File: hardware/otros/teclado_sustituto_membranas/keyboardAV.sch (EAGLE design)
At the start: 98 parts, among them IC1 74HC32, IC2 74LS244DW

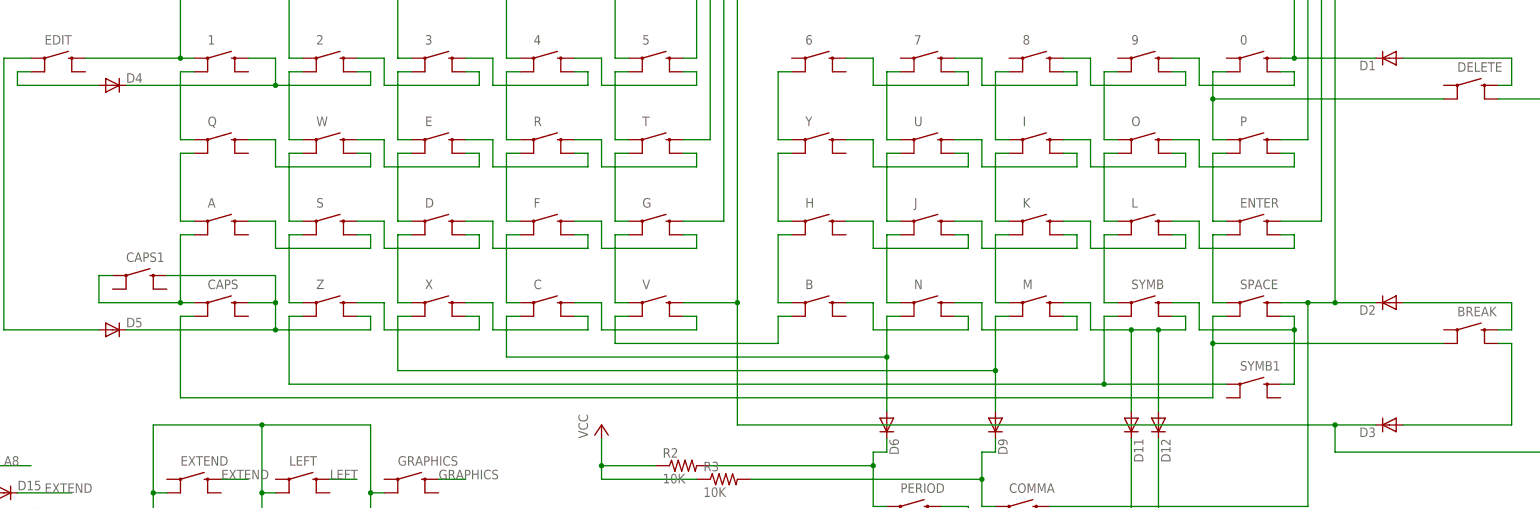
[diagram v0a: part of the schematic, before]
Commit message: 
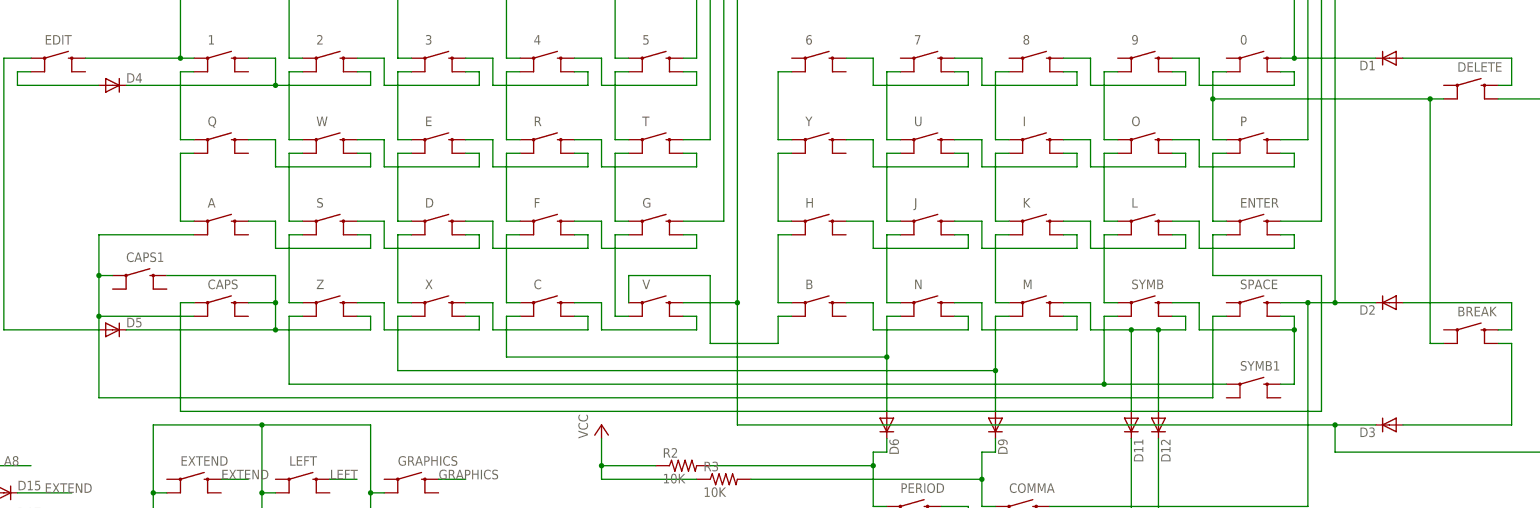
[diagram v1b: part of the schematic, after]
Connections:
- removed net N$52: ENTER.3, SPACE.1
- removed net N$8: A.3, CAPS.1, CAPS1.1
- new net N$91: A.3, CAPS.3, CAPS1.1, SPACE.3
- net N$19: now also V.1; no longer V.3
- net N$28: now also V.3; no longer V.1
- net N$54: now also BREAK.3
- net N$9: now also CAPS.1, ENTER.3; no longer BREAK.3, CAPS.3, SPACE.3

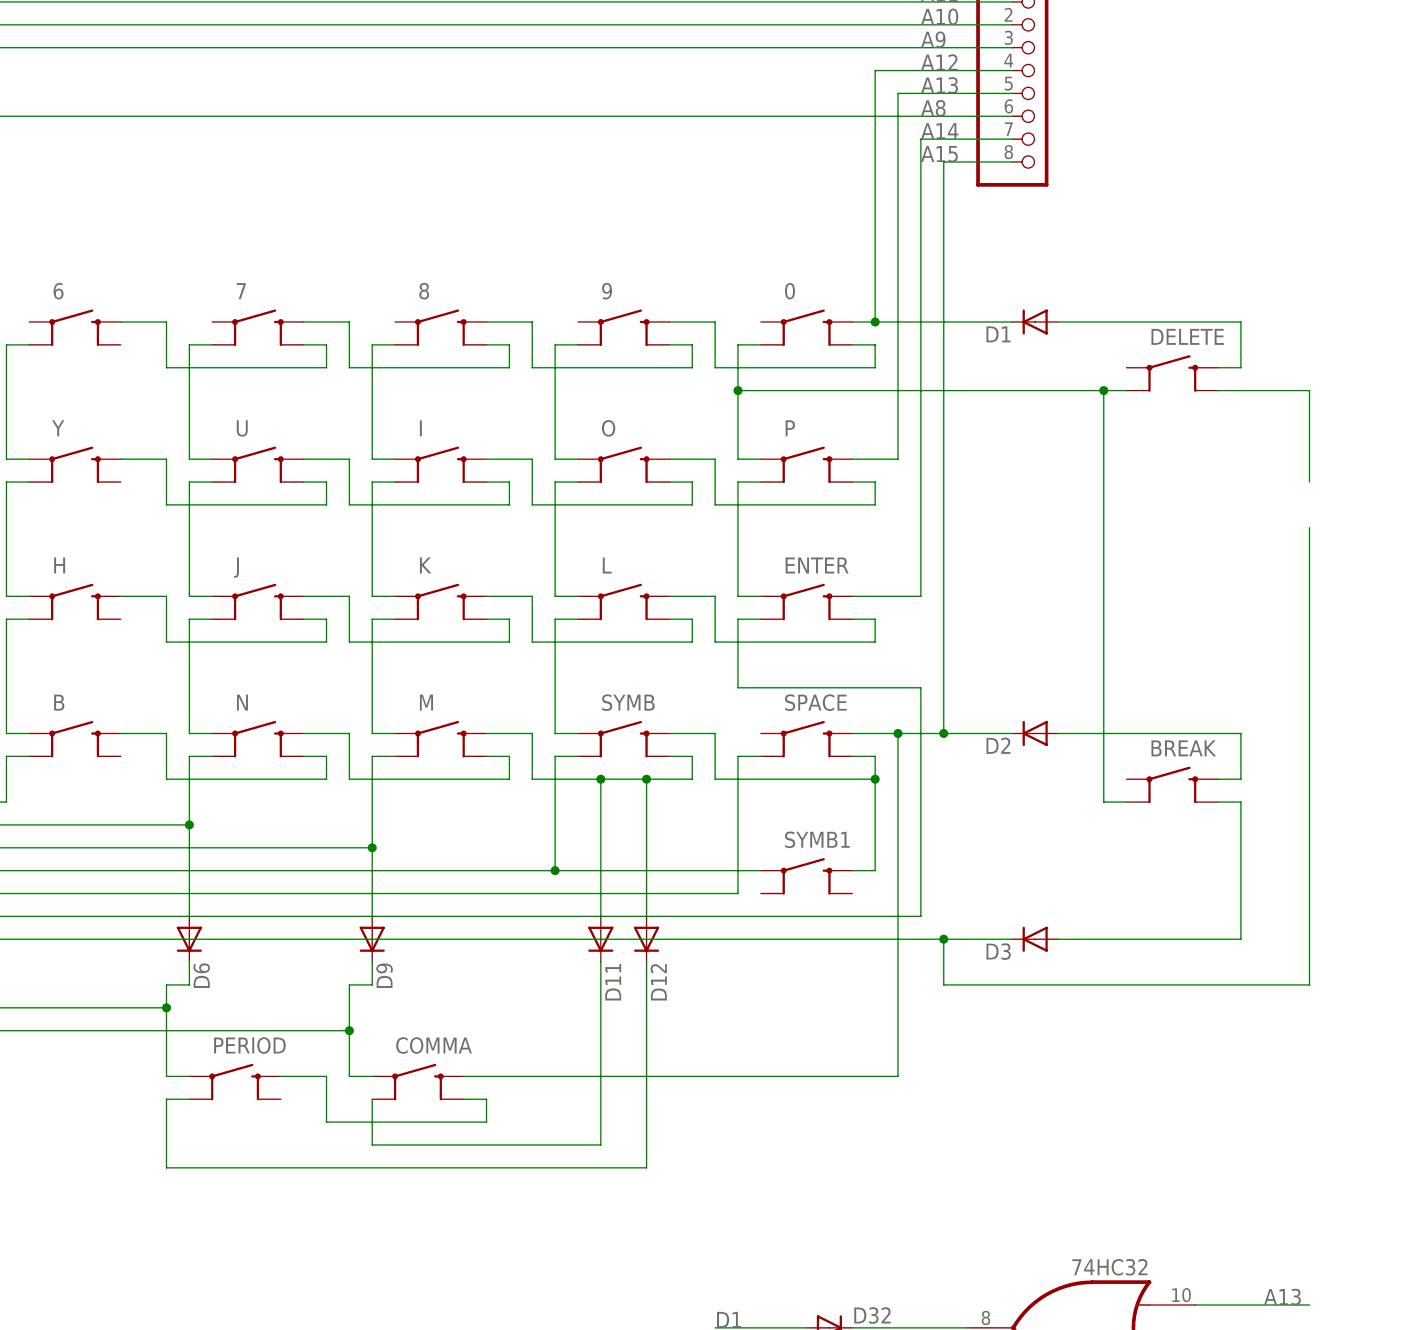
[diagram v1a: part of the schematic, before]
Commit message: 
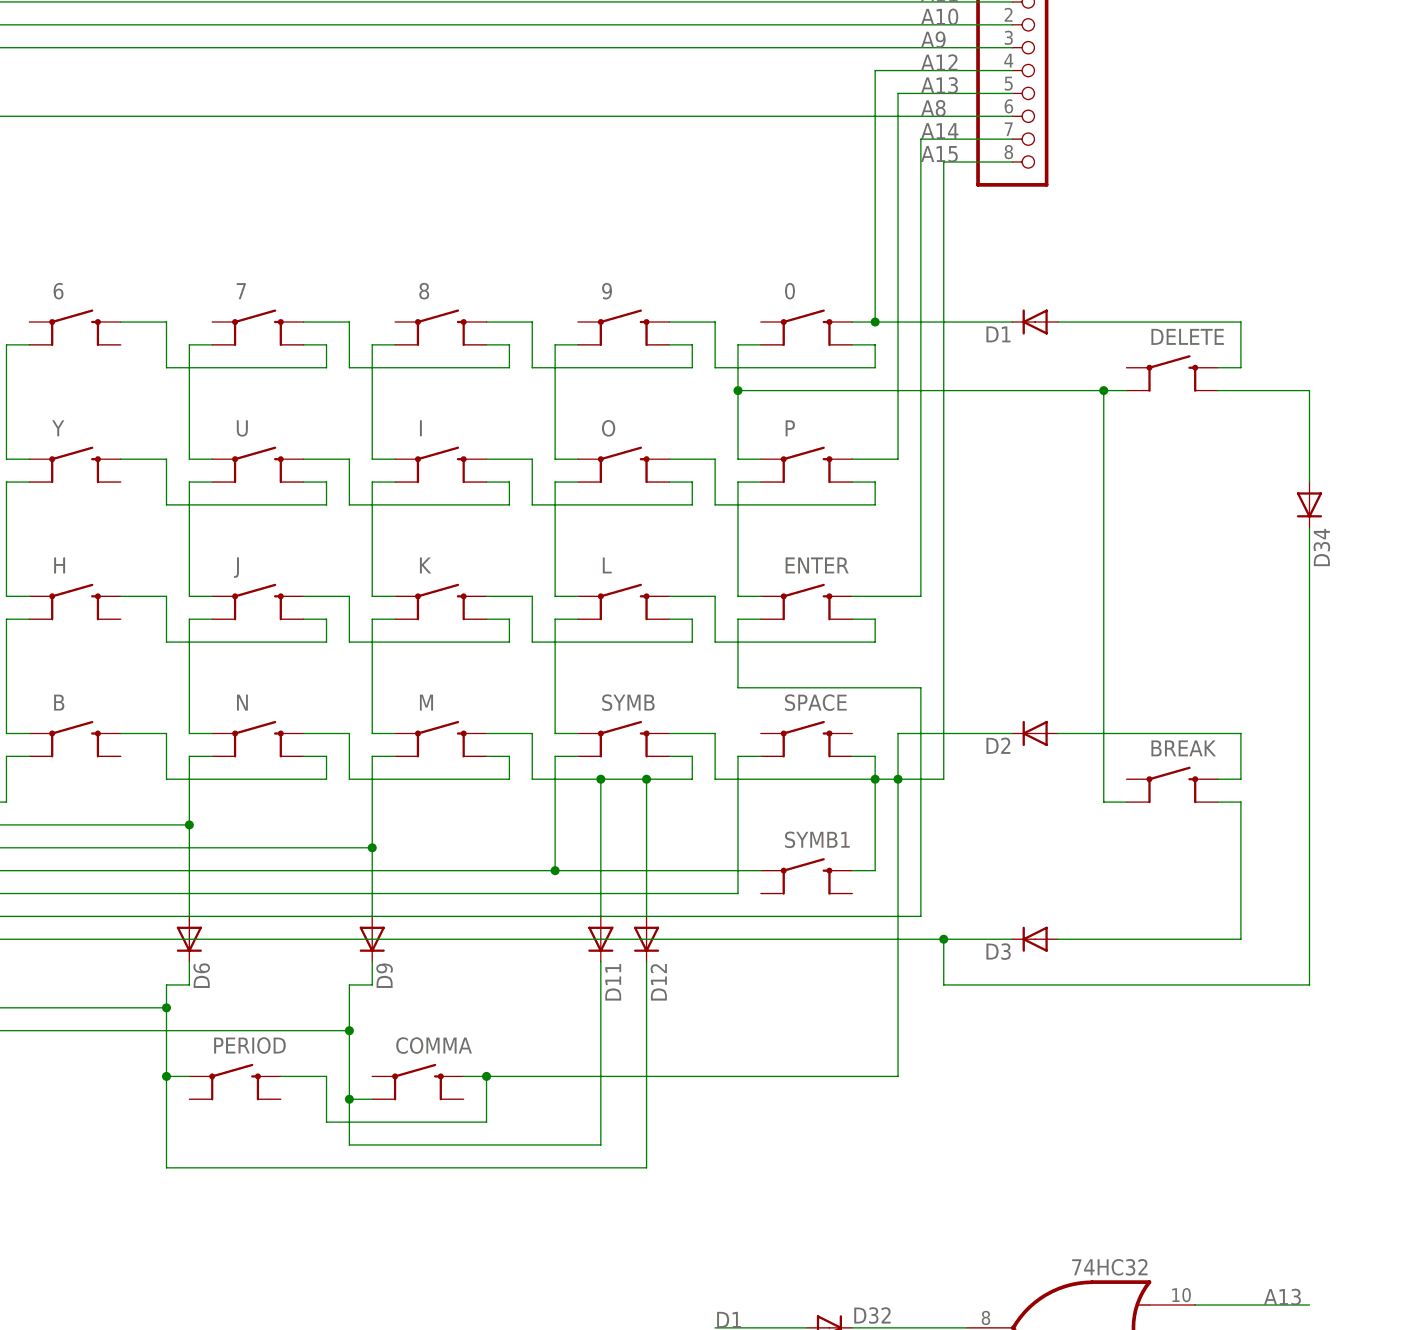
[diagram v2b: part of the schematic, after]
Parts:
- added D34: (no value), diode:DIODE-SOD323-R
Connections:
- removed net N$69: SPACE.4, SYMB.2, SYMB1.2
- removed net N$76: COMMA.4, PERIOD.2
- removed net N$78: COMMA.3, D11.C
- removed net N$82: D6.C, PERIOD.1, R2.2
- net A15: now also PERIOD.2, SPACE.4, SYMB.2, SYMB1.2; no longer SPACE.2
- net A8: now also D34.C
- net N$73: now also D34.A
- net N$79: now also D6.C, PERIOD.1, R2.2; no longer PERIOD.3
- net N$83: now also COMMA.3, D11.C; no longer COMMA.1
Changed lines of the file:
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@@
 <part name="INVV" library="SparkFun-Electromechanical" deviceset="SWITCH-MOMENTARY-2" device="SMD" value=""/>
 <part name="RIGHT" library="SparkFun-Electromechanical" deviceset="SWITCH-MOMENTARY-2" device="SMD" value=""/>
+<part name="D34" library="diode" deviceset="DIODE-" device="SOD323-R"/>
 </parts>
 <sheets>
@@
 <instance part="INVV" gate="G$1" x="-99.06" y="-45.72"/>
 <instance part="RIGHT" gate="G$1" x="-78.74" y="-45.72"/>
+<instance part="D34" gate="G$1" x="154.94" y="58.42" rot="R270"/>
 </instances>
 <busses>
@@
 <pinref part="D3" gate="G$1" pin="C"/>
 <pinref part="V" gate="G$1" pin="2"/>
+<pinref part="D34" gate="G$1" pin="C"/>
 </segment>
 <segment>
@@
 <net name="A15" class="0">
 <segment>
-<pinref part="JP2" gate="A" pin="8"/>
-<wire x1="121.92" y1="96.52" x2="114.3" y2="96.52" width="0.1524" layer="91"/>
-<wire x1="114.3" y1="96.52" x2="114.3" y2="33.02" width="0.1524" layer="91"/>
-<wire x1="114.3" y1="33.02" x2="109.22" y2="33.02" width="0.1524" layer="91"/>
-<label x="111.76" y="96.52" size="1.778" layer="95"/>
-<wire x1="109.22" y1="33.02" x2="104.14" y2="33.02" width="0.1524" layer="91"/>
-<wire x1="121.92" y1="33.02" x2="114.3" y2="33.02" width="0.1524" layer="91"/>
-<junction x="114.3" y="33.02"/>
-<wire x1="60.96" y1="-5.08" x2="109.22" y2="-5.08" width="0.1524" layer="91"/>
-<wire x1="109.22" y1="-5.08" x2="109.22" y2="33.02" width="0.1524" layer="91"/>
-<junction x="109.22" y="33.02"/>
-<pinref part="D2" gate="G$1" pin="C"/>
-<pinref part="SPACE" gate="G$1" pin="2"/>
-<pinref part="COMMA" gate="G$1" pin="2"/>
-</segment>
-<segment>
 <wire x1="-142.24" y1="-50.8" x2="-129.54" y2="-50.8" width="0.1524" layer="91"/>
 <label x="-134.62" y="-50.8" size="1.778" layer="95"/>
 <pinref part="IC1" gate="B" pin="I1"/>
+</segment>
+<segment>
+<pinref part="JP2" gate="A" pin="8"/>
+<wire x1="121.92" y1="96.52" x2="114.3" y2="96.52" width="0.1524" layer="91"/>
+<wire x1="114.3" y1="96.52" x2="114.3" y2="27.94" width="0.1524" layer="91"/>
+<label x="111.76" y="96.52" size="1.778" layer="95"/>
+<wire x1="104.14" y1="30.48" x2="106.68" y2="30.48" width="0.1524" layer="91"/>
+<wire x1="106.68" y1="30.48" x2="106.68" y2="27.94" width="0.1524" layer="91"/>
+<wire x1="106.68" y1="27.94" x2="88.9" y2="27.94" width="0.1524" layer="91"/>
+<wire x1="88.9" y1="27.94" x2="88.9" y2="33.02" width="0.1524" layer="91"/>
+<wire x1="88.9" y1="33.02" x2="83.82" y2="33.02" width="0.1524" layer="91"/>
+<wire x1="104.14" y1="17.78" x2="106.68" y2="17.78" width="0.1524" layer="91"/>
+<wire x1="106.68" y1="17.78" x2="106.68" y2="27.94" width="0.1524" layer="91"/>
+<junction x="106.68" y="27.94"/>
+<pinref part="SYMB" gate="G$1" pin="2"/>
+<pinref part="SPACE" gate="G$1" pin="4"/>
+<pinref part="SYMB1" gate="G$1" pin="2"/>
+<wire x1="114.3" y1="27.94" x2="109.22" y2="27.94" width="0.1524" layer="91"/>
+<wire x1="109.22" y1="27.94" x2="106.68" y2="27.94" width="0.1524" layer="91"/>
+<wire x1="121.92" y1="33.02" x2="109.22" y2="33.02" width="0.1524" layer="91"/>
+<wire x1="60.96" y1="-5.08" x2="63.5" y2="-5.08" width="0.1524" layer="91"/>
+<wire x1="63.5" y1="-5.08" x2="109.22" y2="-5.08" width="0.1524" layer="91"/>
+<wire x1="109.22" y1="-5.08" x2="109.22" y2="27.94" width="0.1524" layer="91"/>
+<pinref part="D2" gate="G$1" pin="C"/>
+<pinref part="COMMA" gate="G$1" pin="2"/>
+<junction x="109.22" y="27.94"/>
+<wire x1="109.22" y1="27.94" x2="109.22" y2="33.02" width="0.1524" layer="91"/>
+<wire x1="63.5" y1="-10.16" x2="45.72" y2="-10.16" width="0.1524" layer="91"/>
+<wire x1="45.72" y1="-10.16" x2="45.72" y2="-5.08" width="0.1524" layer="91"/>
+<wire x1="45.72" y1="-5.08" x2="40.64" y2="-5.08" width="0.1524" layer="91"/>
+<pinref part="PERIOD" gate="G$1" pin="2"/>
+<wire x1="63.5" y1="-10.16" x2="63.5" y2="-5.08" width="0.1524" layer="91"/>
+<junction x="63.5" y="-5.08"/>
 </segment>
 </net>
@@
 <pinref part="H" gate="G$1" pin="2"/>
 <pinref part="J" gate="G$1" pin="4"/>
-</segment>
-</net>
-<net name="N$69" class="0">
-<segment>
-<wire x1="104.14" y1="30.48" x2="106.68" y2="30.48" width="0.1524" layer="91"/>
-<wire x1="106.68" y1="30.48" x2="106.68" y2="27.94" width="0.1524" layer="91"/>
-<wire x1="106.68" y1="27.94" x2="88.9" y2="27.94" width="0.1524" layer="91"/>
-<wire x1="88.9" y1="27.94" x2="88.9" y2="33.02" width="0.1524" layer="91"/>
-<wire x1="88.9" y1="33.02" x2="83.82" y2="33.02" width="0.1524" layer="91"/>
-<wire x1="104.14" y1="17.78" x2="106.68" y2="17.78" width="0.1524" layer="91"/>
-<wire x1="106.68" y1="17.78" x2="106.68" y2="27.94" width="0.1524" layer="91"/>
-<junction x="106.68" y="27.94"/>
-<pinref part="SYMB" gate="G$1" pin="2"/>
-<pinref part="SPACE" gate="G$1" pin="4"/>
-<pinref part="SYMB1" gate="G$1" pin="2"/>
 </segment>
 </net>
@@
 <wire x1="154.94" y1="71.12" x2="154.94" y2="60.96" width="0.1524" layer="91"/>
 <pinref part="DELETE" gate="G$1" pin="4"/>
-</segment>
-</net>
-<net name="N$76" class="0">
-<segment>
-<wire x1="60.96" y1="-7.62" x2="63.5" y2="-7.62" width="0.1524" layer="91"/>
-<wire x1="63.5" y1="-7.62" x2="63.5" y2="-10.16" width="0.1524" layer="91"/>
-<wire x1="63.5" y1="-10.16" x2="45.72" y2="-10.16" width="0.1524" layer="91"/>
-<wire x1="45.72" y1="-10.16" x2="45.72" y2="-5.08" width="0.1524" layer="91"/>
-<wire x1="45.72" y1="-5.08" x2="40.64" y2="-5.08" width="0.1524" layer="91"/>
-<pinref part="PERIOD" gate="G$1" pin="2"/>
-<pinref part="COMMA" gate="G$1" pin="4"/>
-</segment>
-</net>
-<net name="N$78" class="0">
-<segment>
-<wire x1="50.8" y1="-7.62" x2="50.8" y2="-12.7" width="0.1524" layer="91"/>
-<wire x1="50.8" y1="-12.7" x2="76.2" y2="-12.7" width="0.1524" layer="91"/>
-<wire x1="76.2" y1="-12.7" x2="76.2" y2="7.62" width="0.1524" layer="91"/>
-<pinref part="D11" gate="G$1" pin="C"/>
-<pinref part="COMMA" gate="G$1" pin="3"/>
+<pinref part="D34" gate="G$1" pin="A"/>
 </segment>
 </net>
 <net name="N$79" class="0">
 <segment>
-<wire x1="30.48" y1="-7.62" x2="27.94" y2="-7.62" width="0.1524" layer="91"/>
-<wire x1="27.94" y1="-7.62" x2="27.94" y2="-15.24" width="0.1524" layer="91"/>
+<wire x1="27.94" y1="-5.08" x2="27.94" y2="-15.24" width="0.1524" layer="91"/>
 <wire x1="27.94" y1="-15.24" x2="81.28" y2="-15.24" width="0.1524" layer="91"/>
 <wire x1="81.28" y1="-15.24" x2="81.28" y2="7.62" width="0.1524" layer="91"/>
 <pinref part="D12" gate="G$1" pin="C"/>
-<pinref part="PERIOD" gate="G$1" pin="3"/>
-</segment>
-</net>
-<net name="N$82" class="0">
-<segment>
 <wire x1="30.48" y1="7.62" x2="30.48" y2="5.08" width="0.1524" layer="91"/>
 <wire x1="30.48" y1="5.08" x2="27.94" y2="5.08" width="0.1524" layer="91"/>
@@
 <pinref part="D6" gate="G$1" pin="C"/>
 <pinref part="PERIOD" gate="G$1" pin="1"/>
+<junction x="27.94" y="-5.08"/>
 </segment>
 </net>
@@
 <wire x1="50.8" y1="5.08" x2="48.26" y2="5.08" width="0.1524" layer="91"/>
 <wire x1="48.26" y1="5.08" x2="48.26" y2="0" width="0.1524" layer="91"/>
-<wire x1="48.26" y1="0" x2="48.26" y2="-5.08" width="0.1524" layer="91"/>
-<wire x1="48.26" y1="-5.08" x2="50.8" y2="-5.08" width="0.1524" layer="91"/>
 <wire x1="5.08" y1="0" x2="48.26" y2="0" width="0.1524" layer="91"/>
 <junction x="48.26" y="0"/>
 <pinref part="R3" gate="G$1" pin="2"/>
 <pinref part="D9" gate="G$1" pin="C"/>
-<pinref part="COMMA" gate="G$1" pin="1"/>
-</segment>
-</net>
+<wire x1="48.26" y1="-12.7" x2="76.2" y2="-12.7" width="0.1524" layer="91"/>
+<wire x1="76.2" y1="-12.7" x2="76.2" y2="7.62" width="0.1524" layer="91"/>
+<pinref part="D11" gate="G$1" pin="C"/>
+<wire x1="48.26" y1="0" x2="48.26" y2="-7.62" width="0.1524" layer="91"/>
+<pinref part="COMMA" gate="G$1" pin="3"/>
+<wire x1="48.26" y1="-7.62" x2="48.26" y2="-12.7" width="0.1524" layer="91"/>
+<wire x1="50.8" y1="-7.62" x2="48.26" y2="-7.62" width="0.1524" layer="91"/>
+<junction x="48.26" y="-7.62"/>
+</segment>
+</net>
